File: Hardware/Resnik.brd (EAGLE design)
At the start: 64.8 x 100 mm, 178 parts, among them IC1 ATMEGA644M, J1 CONN_82.54_SCREW, J3 CONN_82.54_SCREW, J4 CONN_42.54_SCREW, Q1 DMG3404, Q2 DMG3404, Q3 FDN360P, Q4 FDN360P, Q5 FDN360P, Q6 DMG3404, U1 TLV61220DBV, U10 SN74AUP1G04YFP, U11 SN74AUP2G86SOT833-1, U12 SN74AUP2G08DQE, U13 SN74AUP2G08DQE, U14 SN74AUP2G08DQE, U15 MIC2039MT, U16 MIC2039MT, U17 MIC2039MT, U18 MIC2039MT, U19 TPS22917DBV, U2 TPS62822DLC, U20 TPS22917DBV, U21 TXS0102DQM, U22 BME280, U23 FT231X-Q, U24 TPS22917DBV, U25 TXS0108RGY, U26 TXS0108RGY, U27 TXS0104RGY, U28 MCP4726A2SOT-23, U29 ADS1115, U3 TPS61032RSA, U30 ADS1115, U31 INA211DCK, U32 INA210DCK, U33 TCA9555RTW, U5 BQ2980RUG, U6 TPS2105, U7 LTC4412S6, U8 TPS79733, U9 SN74AUP1G04YFP

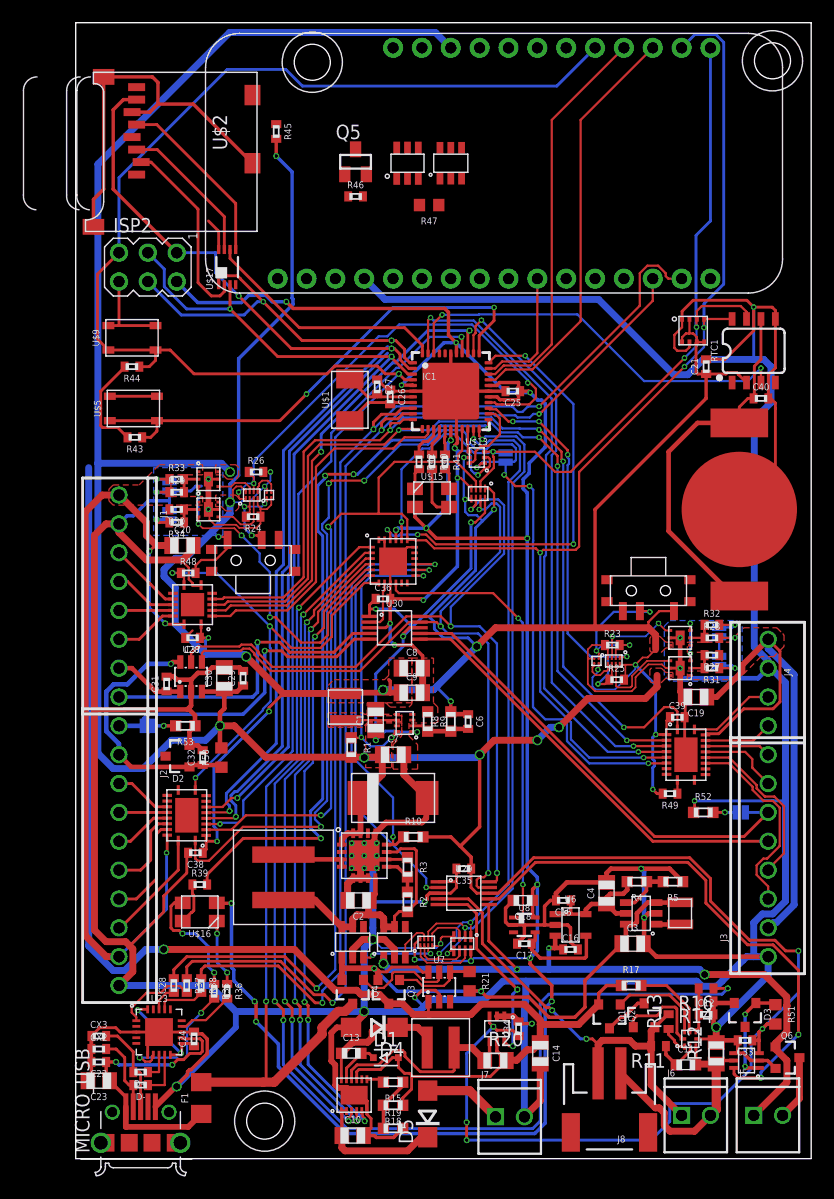
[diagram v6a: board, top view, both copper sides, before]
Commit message: Layout tentative completed, sent to DFM check
Layout complete for v0.0, pending final triple check, sent to DFM check to verify manufacture issues. Ready for final external review.
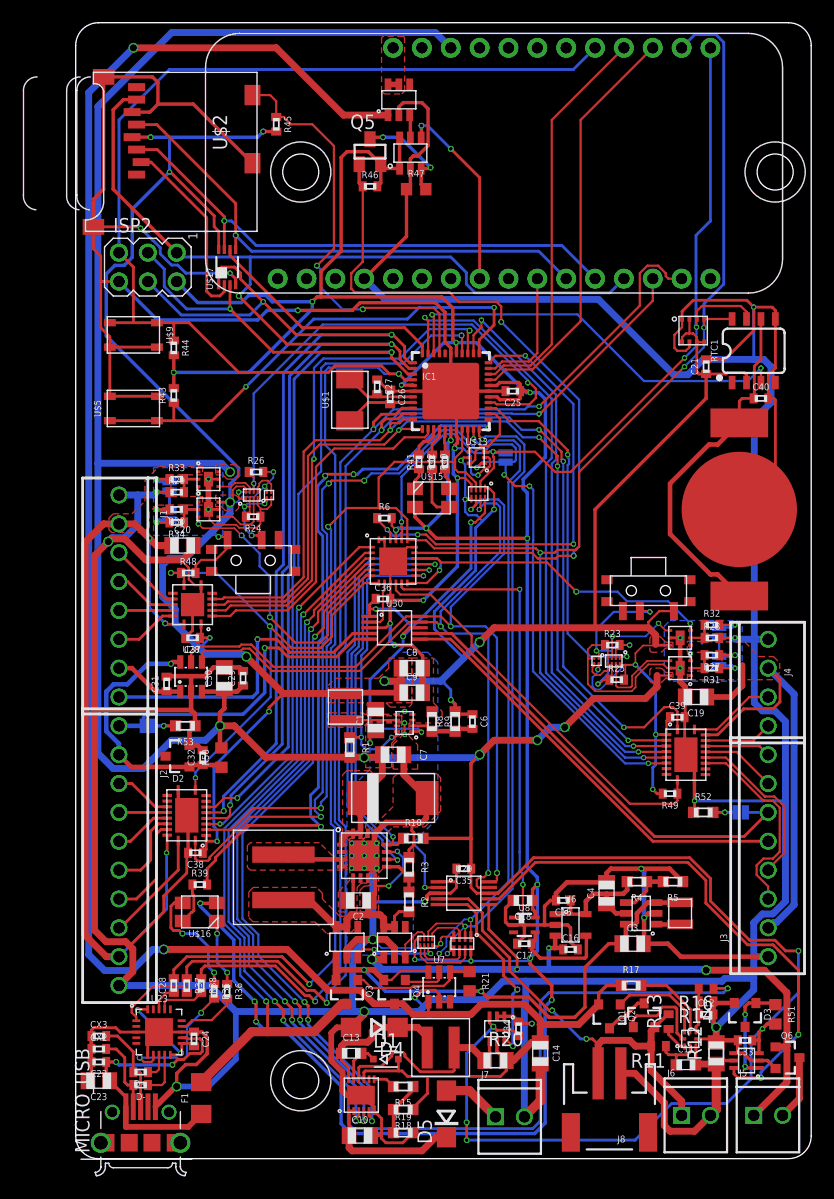
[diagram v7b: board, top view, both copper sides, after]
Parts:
- removed H1: (no value), bschulz:4_40
- added H4: (no value), bschulz:4_40
- added R6: 10k, bschulz_passives:R0402
- added U$4: (no value), awickert:NWLOGO_MED
- moved H2 9.79 mm to (61.6, 86.9)
- moved U24 7.22 mm to (28.4, 93.2)
- moved R43 5.03 mm to (8.64, 67.2), turned to 90 degrees
- moved H3 4.77 mm to (19.8, 6.86)
- moved R44 4.04 mm to (8.64, 71.4), turned to 270 degrees
- moved Q3 3.68 mm to (23.9, 14.7)
- moved Q4 3.68 mm to (28.1, 14.7)
- moved R47 1.81 mm to (30.0, 85.3), turned to 0 degrees
- moved D5 1.65 mm to (32.6, 3.94)
- moved Q5 1.55 mm to (25.9, 88.6)
- moved R46 1.55 mm to (25.9, 85.6)
- moved R15 0.97 mm to (28.8, 6.35)
- moved R18 0.97 mm to (28.8, 4.32)
- moved R19 0.97 mm to (28.8, 2.29)
- moved U$3 0.92 mm to (29.5, 88.5)
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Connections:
- removed net V_BETA_CTL: U7.3
- new net V_HP_SYNC: U3.10, U33.12
- net 3V3_CORE: now also R6.2
- net BUS_LOGIC_EN_SEC: now also U33.10
- net FAULT_SEC: now also U33.16
- net FEATHER_EN: now also U33.17
- net GLOBAL_INT: now also R6.1
- net GND: now also J1.1, J4.1, U7.3; no longer J1.2, J4.2, U3.10
- net PG_LDO: now also U33.11; no longer U33.10
- net VBUS_PRIME: now also J1.2; no longer J1.1
- net VBUS_SEC: now also J4.2; no longer J4.1
- net VUSB_POWER: now also Q3.3; no longer Q4.3
- net V_LI: now also Q4.3; no longer Q3.3
- net WD_DONE: now also MS1.8
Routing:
- net GND: track 703.0 -> 799.5 mm, vias 20 -> 29
- net FEATHER_EN: track 0.00 -> 64.7 mm, vias 0 -> 2
- net V_LI: track 123.8 -> 187.7 mm, vias 1 -> 2
- net MISO: track 93.2 -> 134.7 mm
- net V_HP_SYNC: track 0.00 -> 40.5 mm, vias 0 -> 2
- net SD_CD: track 0.00 -> 38.1 mm, vias 0 -> 2
- net 3V3_CORE: track 215.1 -> 252.2 mm, vias 16 -> 17
- net MOSI_BUF: track 13.1 -> 47.8 mm, vias 0 -> 1
- net BUS_LOGIC_EN_SEC: track 1.21 -> 35.7 mm
- net SCK_BUF: track 15.6 -> 46.3 mm, vias 0 -> 1
- net 3V3_AUX: track 242.0 -> 271.0 mm, vias 19 -> 21
- net FAULT_SEC: track 3.92 -> 30.5 mm, vias 2 -> 3
- net WD_DONE: track 0.00 -> 17.0 mm, vias 0 -> 2
- net N$63: track 0.00 -> 9.36 mm, vias 0 -> 2
- net VBUS_SEC: track 49.0 -> 41.4 mm
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- added copper zone on layer 1, net FEATHER_BAT
- added copper zone on layer 1, net N$5
- added copper zone on layer 1, net V_HP
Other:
- outline, holes or cut-outs redrawn
- board text added: "+"
- board text added: "-"
- board text added: "2.6~4.475v"
- board text added: "3.3~5.5v"
- board text added: "4.95~32v"
- board text added: "A0"
- board text added: "A1"
- board text added: "CS"
- board text added: "DAC"
- board text added: "GND"
- board text added: "GP0"
- board text added: "GP1"
- board text added: "GP2"
- board text added: "GP3"
- board text added: "J0"
- board text added: "J1"
- board text added: "J2"
- board text added: "J3"
- board text added: "J4"
- board text added: "J5"
- board text added: "J6"
- board text added: "MISO"
- board text added: "MOSI"
- board text added: "Primary Bus"
- board text added: "Project Resnik v0.0 ---------------- Developed by Northern Widget and University of Minnesota"
- board text added: "RX"
- board text added: "SCK"
- board text added: "SCL"
- board text added: "SDA"
- board text added: "Secondary Bus"
- board text added: "TX"
- board text added: "VBat"
- board text added: "VPrime"
- board text added: "VSolar"
- board text added: "Vbus"
- board text added: "Vref"
- board text added: "±"

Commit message: Minor board edits, updated gerbers, pending DFM
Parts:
- removed CX2, CX3: 12pF, bschulz_passives:C0402
- removed D+, D-: 27, bschulz_passives:R0402
- removed H4: (no value), bschulz:4_40
- removed U$13: SN74LVC1G3157DRL, bschulz:DRL_R-PDSO-N6
- removed U$15, U$16: CLVBA-FKA, bschulz:CLVBA-FKA
- removed U$17: SN74AUP3G34DCU, bschulz:DCU_(R-PDSO-G8)
- removed U$3: TPL5111DDC, bschulz:DDC_R-PDSO-G6
- added C41: 12pF, bschulz_passives:C0402
- added C42: 1uF, bschulz_passives:C0402
- added D6, D7: (no value), bschulz:SOT23-3
- added H1: (no value), bschulz:4_40
- added R22: 10k, bschulz_passives:R0402
- added R7: 180k, bschulz_passives:R0603
- added U34: INA211DCK, bschulz:DCK_R-PDSO-G6
- added U35: INA210DCK, bschulz:DCK_R-PDSO-G6
- added U36: TCA9555RTW, bschulz:RTW_S-PWQFN-N24
- C22: value 0.1uF -> 10uF; device bschulz_passives:C0402 -> bschulz_passives:C0805
- C23: value 10uF -> 12pF; device bschulz_passives:C0805 -> bschulz_passives:C0402
- C24: value 0.1uF -> 12pF
- C25: value 1uF -> 0.1uF
- C26, C27: value 12pF -> (none)
- C28, C34: value 0.1uF -> (none)
- C37, C38, C39: value (none) -> 0.1uF
- C40: value (none) -> 12pF
- D1: device bschulz:SOD323-R -> bschulz:DO214AC
- D2: device bschulz:SOT23-3 -> bschulz:SOD323-R
- D3: device bschulz:SOT23-3 -> bschulz:DO214AC
- D4, D5: value (none) -> CLVBA-FKA; device bschulz:DO214AC -> bschulz:CLVBA-FKA
- J3: value CONN_82.54_SCREW -> CONN_42.54_SCREW; device bschulz:1X08_SCREW -> bschulz:1X04_SCREW
- J4: value CONN_42.54_SCREW -> CONN_82.54_SCREW; device bschulz:1X04_SCREW -> bschulz:1X08_SCREW
- Q3: device bschulz:SOT23-3 -> transistor-power:SUPER-SOT3
- Q5: device transistor-power:SUPER-SOT3 -> bschulz:SOT23-3
- R10: value 180k -> 3m; device bschulz_passives:R0603 -> bschulz_passives:R0805
- R11: value 330R -> 20R
- R12: value 3m -> (none); device bschulz_passives:R0805 -> bschulz:R0402
- R13: value 20R -> 91k; device bschulz:R0402 -> bschulz_passives:R0603
- R14: value (none) -> 100R
- R15: value 91k -> 2k
- R16: value 100R -> 182k; device bschulz:R0402 -> bschulz_passives:R0603
- R17: value 2k -> 330k
- R18: value 182k -> 5m; device bschulz_passives:R0603 -> bschulz_passives:R0805
- R19: value 330k -> 180k; device bschulz_passives:R0603 -> bschulz_passives:R0402
- R20: value 5m -> 120k; device bschulz_passives:R0805 -> bschulz:R0603
- R26: value 10k -> 287R
- R34: value 287R -> 27
- R35: value 330 -> 27
- R41: value 330 -> 10k
- R43, R44: value 10k -> 330
- R46: value 180k -> 10k
- R47: value 120k -> 10k; device bschulz:R0603 -> bschulz_passives:R0402
- R48: value 10k -> 330R; device bschulz_passives:R0402 -> bschulz:R0603
- R49: device bschulz_passives:R0402 -> bschulz_passives:R0603
- R50: value 330R -> 10k; device bschulz:R0603 -> bschulz_passives:R0603
- R52, R53: device bschulz_passives:R0603 -> bschulz_passives:R0402
- R6: value 10k -> 820k; device bschulz_passives:R0402 -> bschulz_passives:R0603
- R8: value 820k -> 180k
- R9: value 180k -> 330R; device bschulz_passives:R0603 -> bschulz:R0402
- U10: value SN74AUP1G04YFP -> TPS22917DBV; device bschulz:DSBGD_4 -> bschulz:DBV_R-PDSO-G6
- U11: value SN74AUP2G86SOT833-1 -> SN74AUP1G04YFP; device bschulz:SOT833-1 -> bschulz:DSBGD_4
- U12: value SN74AUP2G08DQE -> SN74AUP1G04YFP; device bschulz:DQE_R-PX2SON-N8 -> bschulz:DSBGD_4
- U13: value SN74AUP2G08DQE -> SN74AUP2G86SOT833-1; device bschulz:DQE_R-PX2SON-N8 -> bschulz:SOT833-1
- U15, U16: value MIC2039MT -> SN74AUP2G08DQE; device bschulz:DFN_6_2X2 -> bschulz:DQE_R-PX2SON-N8
- U19, U20: value TPS22917DBV -> MIC2039MT; device bschulz:DBV_R-PDSO-G6 -> bschulz:DFN_6_2X2
- U21: value TXS0102DQM -> TPS22917DBV; device bschulz:DQM_R-PX2SON-N8 -> bschulz:DBV_R-PDSO-G6
- U22: value BME280 -> TPS22917DBV; device bschulz:BME280 -> bschulz:DBV_R-PDSO-G6
- U24: value TPS22917DBV -> SN74LVC1G3157DRL; device bschulz:DBV_R-PDSO-G6 -> bschulz:DRL_R-PDSO-N6
- U25: value TXS0108RGY -> SN74AUP3G34DCU; device bschulz:RGY_S-PVQFN-N20 -> bschulz:DCU_(R-PDSO-G8)
- U26: value TXS0108RGY -> TXS0102DQM; device bschulz:RGY_S-PVQFN-N20 -> bschulz:DQM_R-PX2SON-N8
- U27: value TXS0104RGY -> TXS0108RGY; device bschulz:RGY_S-PVQFN-N14 -> bschulz:RGY_S-PVQFN-N20
- U28: value MCP4726A2SOT-23 -> TXS0108RGY; device bschulz:SOT23-6L -> bschulz:RGY_S-PVQFN-N20
- U29: value ADS1115 -> TXS0104RGY; device bschulz:VSSOP_10 -> bschulz:RGY_S-PVQFN-N14
- U30: value ADS1115 -> MCP4726A2SOT-23; device bschulz:VSSOP_10 -> bschulz:SOT23-6L
- U31: value INA211DCK -> BME280; device bschulz:DCK_R-PDSO-G6 -> bschulz:BME280
- U32: value INA210DCK -> ADS1115; device bschulz:DCK_R-PDSO-G6 -> bschulz:VSSOP_10
- U33: value TCA9555RTW -> ADS1115; device bschulz:RTW_S-PWQFN-N24 -> bschulz:VSSOP_10
- U8: value TPS79733 -> TPL5111DDC; device bschulz:DCK_R-PDSO-G5 -> bschulz:DDC_R-PDSO-G6
- U9: value SN74AUP1G04YFP -> TPS79733; device bschulz:DSBGD_4 -> bschulz:DCK_R-PDSO-G5
- moved H2 90.2 mm to (19.8, 6.86)
- moved R19 83.4 mm to (25.9, 85.6)
- moved C21 81.3 mm to (2.03, 8.51), turned to 180 degrees
- moved H3 80.0 mm to (19.8, 86.9)
- moved R20 77.0 mm to (30.0, 85.3)
- moved Q5 73.9 mm to (28.1, 14.7), turned to 180 degrees
- moved Q3 73.9 mm to (25.9, 88.6), turned to 0 degrees
- moved U8 68.7 mm to (29.5, 88.5), turned to 0 degrees
- moved U31 64.4 mm to (54.4, 72.9)
- moved C25 63.6 mm to (10.4, 10.5), turned to 90 degrees
- moved R52 62.0 mm to (8.64, 71.4), turned to 270 degrees
- moved U22 61.9 mm to (23.9, 19.1), turned to 0 degrees
- moved C37 60.2 mm to (58.9, 10.4)
- moved C33 59.8 mm to (8.00, 41.8), turned to 90 degrees
- moved C34 59.5 mm to (60.3, 66.9), turned to 0 degrees
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- renumbered ISP2 to ISP1, MICRO_USB to USB1, U$1 to XTAL1, U$2 to SD1, U$5 to S3, U$9 to S4
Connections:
- new net N$1: USB1.BODY@1, USB1.BODY@2, USB1.BODY@3, USB1.BODY@4, USB1.BODY@7, USB1.BODY@8
- net 3V3_AUX: now also C26.1, C27.1, C28.1, C32.1, R24.2, R41.2, R46.2, R47.2, R6.2, U11.A2, U12.A2, U14.8, U15.8, U20.6, U24.5, U25.8, U26.1, U26.5, U27.2, U28.2, U29.1, U31.2, U31.5, U31.6, U31.8; no longer C21.1, C37.1, C38.1, C39.1, R26.2, R45.2, R48.2, R49.2, R8.2, U$13.5, U$17.8, U10.A2, U12.8, U13.8, U16.6, U21.1, U21.5, U22.2, U22.5, U22.6, U22.8, U25.2, U26.2, U27.1, U9.A2
- net 3V3_AUX_PG: now also U36.13; no longer U33.13
- net 3V3_CORE: now also C42.1, D4.2, D5.2, Q3.2, R19.2, R45.2, R52.2, R53.2, U13.8, U16.8, U36.21, U8.1, U8.6, U9.5; no longer C25.1, Q5.2, R43.2, R44.2, R46.2, R6.2, U$15.2, U$16.2, U$3.1, U$3.6, U11.8, U14.8, U33.21, U8.5
- net 3V3_FTDI: now also C25.1; no longer C24.1
- net 5V_AUX: now also C37.1, C38.1, R48.2, R8.2, U19.6, U26.8, U30.3, U32.8, U33.1, U33.8, U34.3, U35.3; no longer C33.1, C34.1, R10.2, R50.2, U15.6, U21.8, U28.3, U29.8, U30.1, U30.8, U31.3, U32.3
- net ADC_0: now also JP6.1, U33.5; no longer JP7.1, U30.5
- net ADC_1: now also U33.4; no longer U30.4
- net ADC_2: now also J4.5, U33.6; no longer J3.5, U30.6
- net ADC_3: now also J4.6, JP7.1, U33.7; no longer J3.6, JP6.1, U30.7
- net ADC_EXT_ALERT: now also U33.2, U36.8; no longer U30.2, U33.8
- net ADC_OB_ALERT: now also U32.2, U36.15; no longer U29.2, U33.15
- net ALIVE_LED: now also R37.2; no longer R39.2
- net BMS_CTR: now also R14.1, U36.2; no longer R16.1, U33.2
- net BUS_LOGIC_EN_PRIME: now also R46.1, U27.10, U29.8, U36.7; no longer R48.1, U25.10, U27.8, U33.7
- net BUS_LOGIC_EN_SEC: now also R47.1, U28.10, U36.10; no longer R49.1, U26.10, U33.10
- net C0: now also U13.1, U13.6, U16.2; no longer U11.1, U11.6, U14.2
- net C1: now also U13.2, U13.5, U16.6; no longer U11.2, U11.5, U14.6
- net CS_EXT: now also U27.4; no longer U25.4
- net CS_OUT: now also U27.17; no longer U25.17
- net DAC_OUT: now also C33.1, U30.1; no longer C31.1, U28.1
- net DTR: now also C39.1; no longer C28.1
- net EN_BUS_PRIME: now also R25.1, U15.1, U15.6; no longer R26.1, U13.1, U13.6
- net EN_BUS_SEC: now also R24.1, U14.1, U14.6; no longer R25.1, U12.1, U12.6
- net FAULT_PRIME: now also U19.3, U20.3, U36.6; no longer U17.3, U18.3, U33.6
- net FAULT_SEC: now also U17.3, U18.3, U36.16; no longer U15.3, U16.3, U33.16
- net FEATHER_BAT: now also U10.5, U10.6; no longer U24.5, U24.6
- net FEATHER_EN: now also Q3.1, R19.1, U36.17; no longer Q5.1, R46.1, U33.17
- net GLOBAL_INT: now also R53.1, U36.22; no longer R6.1, U33.22
- net GND: now also C23.1, C24.1, C26.2, C27.2, C28.2, C40.1, C41.1, C42.2, D3.A, D6.2, D7.2, R10.2, R12.1, R17.2, R20.1, R22.1, R26.1, R27.2, R28.1, R29.2, R49.1, R50.1, R7.1, U10.2, U11.B1, U12.B1, U15.4, U16.4, U19.5, U19.PAD, U19.PAD@1, U20.5, U20.PAD, U20.PAD@1, U21.2, U22.2, U25.4, U26.4, U27.11, U28.11, U28.EP, U29.7, U29.EP, U30.2, U31.1, U31.7, U32.3, U33.3, U34.2, U34.4, U35.1, U35.2, U36.18, U36.23, U36.24, U36.9, U36.EP, U9.2; no longer C23.2, C24.2, C26.1, C27.1, C39.2, C40.2, CX2.1, CX3.1, D2.2, D3.2, D4.A, R12.2, R14.1, R19.2, R24.1, R27.1, R28.2, R29.1, R30.2, R47.1, R52.1, R53.1, R9.1, U$13.2, U$17.4, U$3.2, U10.B1, U11.4, U12.4, U15.5, U15.PAD, U15.PAD@1, U16.5, U16.PAD, U16.PAD@1, U19.2, U20.2, U21.4, U22.1, U22.7, U25.11, U25.EP, U26.11, U26.EP, U27.7, U28.2, U29.1, U29.3, U30.3, U31.2, U31.4, U32.2, U33.18, U33.23, U33.24, U33.9, U33.EP, U9.B1
- net GPIO_0: now also U29.2; no longer U27.2
- net GPIO_0_OUT: now also U29.13; no longer U27.13
- net GPIO_1: now also U29.3; no longer U27.3
- net GPIO_1_OUT: now also U29.12; no longer U27.12
- net GPIO_2: now also U28.5; no longer U26.5
- net GPIO_2_OUT: now also J4.7, U28.16; no longer J3.7, U26.16
- net GPIO_3: now also U28.4; no longer U26.4
- net GPIO_3_OUT: now also J4.8, U28.17; no longer J3.8, U26.17
- net I_LI: now also U32.7, U34.6; no longer U29.7, U31.6
- net I_SOLAR: now also U32.5, U35.6; no longer U29.5, U32.6
- net LBI: now also R8.1, U36.14; no longer R10.1, U33.14
- net LED1: now also R44.1; no longer R42.1
- net LED2: now also R42.1; no longer R40.1
- net LED3: now also R43.1; no longer R41.1
- net LI+: now also R9.2, U32.4; no longer R13.2, U29.4
- net LI-: now also R10.1, U34.5; no longer R12.1, U31.5
- net LOG_INT: now also R45.1; no longer R43.1
- net MISO: now also U27.5; no longer U25.5
- net MISO_OUT: now also U27.16; no longer U25.16
- net MOSI: now also U25.1, U27.6; no longer U$17.1, U25.6
- net MOSI_BUF: now also U25.7; no longer U$17.7
- net MOSI_OUT: now also U27.15; no longer U25.15
- net MPPT_CHRG: now also U36.4; no longer U33.4
- net MPPT_FAULT: now also U36.5; no longer U33.5
- net MPPT_SHDN: now also U36.3; no longer U33.3
- net N$11: now also R15.2; no longer R17.2
- net N$12: now also R13.1, R16.2, R17.1; no longer R15.1, R18.2, R19.1
- net N$13: now also R12.2; no longer R16.2
- net N$14: now also R11.1; no longer R13.1
- net N$15: now also R13.2; no longer R15.2
- net N$16: now also R9.1; no longer R11.1
- net N$18: now also D2.C; no longer D1.C
- net N$20: now also D3.C; no longer D4.C
- net N$21: now also D7.1, U34.1; no longer D3.1, U31.1
- net N$22: now also U13.7, U16.1; no longer U11.7, U14.1
- net N$23: now also U16.7, U21.3; no longer U14.7, U19.3
- net N$24: now also U16.3, U22.3; no longer U14.3, U20.3
- net N$25: now also U13.3, U16.5; no longer U11.3, U14.5
- net N$26: now also U12.B2, U15.5; no longer U10.B2, U13.5
- net N$27: now also R28.2, R32.2, U19.2; no longer R29.2, R33.2, U17.2
- net N$28: now also R23.2, U12.A1, U15.2; no longer R24.2, U10.A1, U13.2
- net N$29: now also U15.7, U19.4; no longer U13.7, U17.4
- net N$3: now also R6.1, R7.2; no longer R8.1, R9.2
- net N$30: now also U15.3, U20.4; no longer U13.3, U18.4
- net N$31: now also R32.1; no longer R33.1
- net N$32: now also R33.2; no longer R34.2
- net N$33: now also R29.1, R33.1, U20.2; no longer R30.1, R34.1, U18.2
- net N$34: now also U11.B2, U14.5; no longer U12.5, U9.B2
- net N$35: now also R22.2, U11.A1, U14.2; no longer R23.2, U12.2, U9.A1
- net N$36: now also U14.7, U17.4; no longer U12.7, U15.4
- net N$37: now also U14.3, U18.4; no longer U12.3, U16.4
- net N$38: now also R26.2, R30.2, U17.2; no longer R27.2, R31.2, U15.2
- net N$39: now also R30.1; no longer R31.1
- net N$40: now also R31.2; no longer R32.2
- net N$41: now also R27.1, R31.1, U18.2; no longer R28.1, R32.1, U16.2
- net N$43: now also C34.1; no longer C40.1
- net N$45: now also Q5.1; no longer Q4.1
- net N$46: now also Q4.1; no longer Q3.1
- net N$47: now also R40.2; no longer R37.2
- net N$48: now also C24.2, R35.2; no longer CX3.2, D+.2
- net N$49: now also C23.2, R34.2; no longer CX2.2, D-.2
- net N$50: now also R35.1; no longer D+.1
- net N$51: now also R39.2; no longer R36.2
- net N$52: now also R34.1; no longer D-.1
- net N$53: now also D4.1, R39.1; no longer R36.1, U$16.1
- net N$54: now also D4.3, R36.1; no longer R35.1, U$16.3
- net N$56: now also D4.4, R37.1; no longer R39.1, U$16.4
- net N$57: now also R36.2; no longer R35.2
- net N$58: now also D5.3, R42.2; no longer R40.2, U$15.3
- net N$59: now also D5.4, R43.2; no longer R41.2, U$15.4
- net N$60: now also D5.1, R44.2; no longer R42.2, U$15.1
- net N$61: now also C40.2; no longer C27.2
- net N$62: now also C41.2; no longer C26.2
- net N$63: now also Q3.3, R20.2, U8.3; no longer Q5.3, R47.2, U$3.3
- net N$64: now also U10.3, U8.5; no longer U$3.5, U24.3
- net N$65: now also JP6.2, R49.2; no longer JP7.2, R53.2
- net N$66: now also JP7.2, R50.2; no longer JP6.2, R52.2
- net N$67: now also D1.C; no longer D5.C
- net PG_LDO: now also U36.11, U9.1; no longer U33.11, U8.1
- net RST: now also C39.2, R52.1; no longer C28.2, R44.1
- net RX_EXT: now also U28.1, U29.5; no longer U26.1, U27.5
- net RX_OUT_PRIME: now also U29.10; no longer U27.10
- net RX_OUT_SEC: now also J3.3, U28.20; no longer J4.3, U26.20
- net SCK: now also U25.3, U27.7; no longer U$17.3, U25.7
- net SCK_BUF: now also U25.5; no longer U$17.5
- net SCK_OUT: now also U27.14; no longer U25.14
- net SCL: now also U26.3, U27.3, U28.6, U31.4, U36.19; no longer U21.3, U22.4, U25.3, U26.6, U33.19
- net SCL_5V: now also U26.6, U30.5, U32.10, U33.10; no longer U21.6, U28.5, U29.10, U30.10
- net SCL_OUT_PRIME: now also U27.18; no longer U25.18
- net SCL_OUT_SEC: now also J4.4, U28.15; no longer J3.4, U26.15
- net SDA: now also U24.4; no longer U$13.4
- net SDA_5V: now also U26.7, U30.4, U32.9, U33.9; no longer U21.7, U28.4, U29.9, U30.9
- net SDA_CTRL: now also U24.6; no longer U$13.6
- net SDA_EXT: now also U24.1, U27.1, U28.7; no longer U$13.1, U25.1, U26.7
- net SDA_OB: now also U24.3, U26.2, U31.3, U36.20; no longer U$13.3, U21.2, U22.3, U33.20
- net SDA_OUT_PRIME: now also U27.20; no longer U25.20
- net SDA_OUT_SEC: now also J4.3, U28.14; no longer J3.3, U26.14
- net SD_CD: now also R41.1; no longer R45.1
- net SD_CS: now also U25.6; no longer U$17.6
- net SD_CS_BUF: now also U25.2; no longer U$17.2
- net SOLAR_SENSE+: now also R18.1, U35.4; no longer R20.1, U32.4
- net TX: now also R40.1; no longer R37.1
- net TX_EXT: now also U28.3, U29.4; no longer U26.3, U27.4
- net TX_OUT_PRIME: now also U29.11; no longer U27.11
- net TX_OUT_SEC: now also J3.4, U28.18; no longer J4.4, U26.18
- net VBUS_PRIME: now also U19.1, U20.1, U27.19, U29.14; no longer U17.1, U18.1, U25.19, U27.14
- net VBUS_SEC: now also U17.1, U18.1, U28.19; no longer U15.1, U16.1, U26.19
- net VREF: now also C31.1, D6.1, R48.1, U30.6; no longer C32.1, D2.1, R50.1, U28.6
- net VUSB: now also C21.1; no longer C23.1
- net VUSB_POWER: now also Q4.3, U36.1; no longer Q3.3, U33.1
- net V_BETA: now also Q5.2, U22.1; no longer Q3.2, U20.1
- net V_CORE: now also U9.4; no longer U8.4
- net V_HP: now also U21.5, U21.6, U22.5, U22.6; no longer U19.5, U19.6, U20.5, U20.6
- net V_HP_SYNC: now also U36.12; no longer U33.12
- net V_LI: now also D2.A, Q5.3, R15.1, R16.1, R18.2, U10.1, U35.5; no longer D1.A, Q4.3, R17.1, R18.1, R20.2, U24.1, U32.5
- net V_PRIME: now also U21.1, U32.6; no longer U19.1, U29.6
- net V_SOLAR: now also D1.A; no longer D5.A
- net WD_DONE: now also U8.4; no longer U$3.4
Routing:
- net N$1: track 0.00 -> 9.00 mm
- net GND: track 799.5 -> 798.2 mm
- net N$43: track 32.1 -> 31.6 mm
